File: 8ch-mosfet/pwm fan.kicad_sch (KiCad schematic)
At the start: 4 parts, among them M1 Fan_4pin

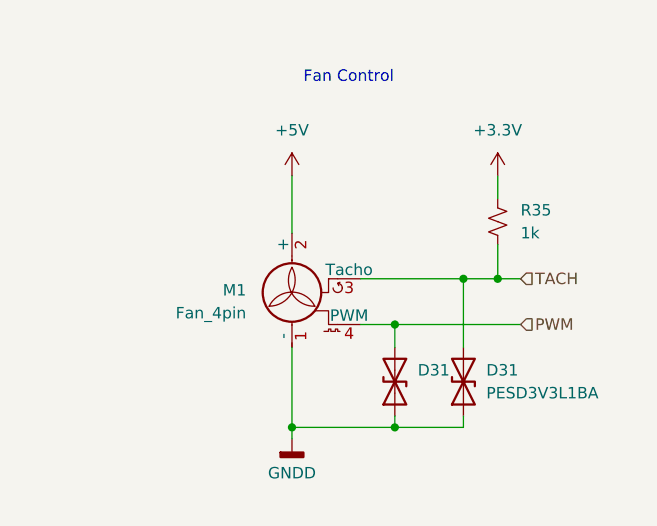
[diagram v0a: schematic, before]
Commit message: changed to MCP3564
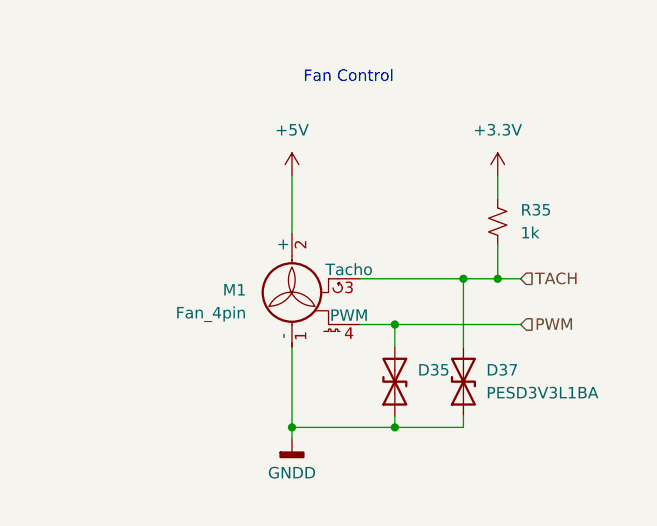
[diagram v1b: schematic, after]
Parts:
- renumbered D31 to D35, D31 to D37

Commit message: more progress on new 8ch board.
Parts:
- added Q17: 2N7002, Package_TO_SOT_SMD:SOT-23, symbol Transistor_FET:2N7002
- added R43: 1k, Resistor_SMD:R_0805_2012Metric_Pad1.20x1.40mm_HandSolder, symbol Device:R_Small_US
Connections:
- net GNDD: now also Q17.2 (S); no longer M1.1 (-)
- new net: M1.1 (-), Q17.3 (D)
- new net: Q17.1 (G), R43.1
- new net MOSFET: R43.2
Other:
- moved on the sheet: D35, D37, M1, R35

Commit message: updated busbar design.
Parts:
- renumbered Q17 to Q18, R43 to R44
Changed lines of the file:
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@@
 		(on_board yes)
 		(dnp no)
-		(property "Reference" "Q17"
+		(property "Reference" "Q18"
 			(at 135.89 95.25 0)
 			(effects
@@
 		(dnp no)
 		(fields_autoplaced yes)
-		(property "Reference" "R43"
+		(property "Reference" "R44"
 			(at 119.38 90.17 90)
 			(effects

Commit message: big update - 12ch, volt adc, senders, etc.
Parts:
- renumbered D35 to D27, D37 to D28, M1 to M2, Q18 to Q34, R44 to R59, R35 to R60
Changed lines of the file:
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@@
 		(dnp no)
 		(fields_autoplaced yes)
-		(property "Reference" "R35"
+		(property "Reference" "R60"
 			(at 161.29 72.39 0)
 			(effects
@@
 			(project "8ch-mosfet"
 				(path "/c83c6236-96e9-46ad-9d7a-9e2efa4a7966/02f6e629-b0e2-41e8-b2e4-f0e125a92a71"
-					(reference "R35")
-					(unit 1)
-				)
-				(path "/c83c6236-96e9-46ad-9d7a-9e2efa4a7966/ad82ad0c-2ba8-4934-bb2a-ed6e11658eb2"
-					(reference "R36")
+					(reference "R60")
+					(unit 1)
+				)
+				(path "/c83c6236-96e9-46ad-9d7a-9e2efa4a7966/ad82ad0c-2ba8-4934-bb2a-ed6e11658eb2"
+					(reference "R58")
 					(unit 1)
 				)
@@
 		(on_board yes)
 		(dnp no)
-		(property "Reference" "D35"
+		(property "Reference" "D27"
 			(at 149.86 95.25 90)
 			(effects
@@
 			(project "8ch-mosfet"
 				(path "/c83c6236-96e9-46ad-9d7a-9e2efa4a7966/02f6e629-b0e2-41e8-b2e4-f0e125a92a71"
-					(reference "D35")
-					(unit 1)
-				)
-				(path "/c83c6236-96e9-46ad-9d7a-9e2efa4a7966/ad82ad0c-2ba8-4934-bb2a-ed6e11658eb2"
-					(reference "D34")
+					(reference "D27")
+					(unit 1)
+				)
+				(path "/c83c6236-96e9-46ad-9d7a-9e2efa4a7966/ad82ad0c-2ba8-4934-bb2a-ed6e11658eb2"
+					(reference "D25")
 					(unit 1)
 				)
@@
 		(dnp no)
 		(fields_autoplaced yes)
-		(property "Reference" "#PWR064"
+		(property "Reference" "#PWR052"
 			(at 158.75 72.39 0)
 			(effects
@@
 			(project "8ch-mosfet"
 				(path "/c83c6236-96e9-46ad-9d7a-9e2efa4a7966/02f6e629-b0e2-41e8-b2e4-f0e125a92a71"
-					(reference "#PWR064")
-					(unit 1)
-				)
-				(path "/c83c6236-96e9-46ad-9d7a-9e2efa4a7966/ad82ad0c-2ba8-4934-bb2a-ed6e11658eb2"
-					(reference "#PWR066")
+					(reference "#PWR052")
+					(unit 1)
+				)
+				(path "/c83c6236-96e9-46ad-9d7a-9e2efa4a7966/ad82ad0c-2ba8-4934-bb2a-ed6e11658eb2"
+					(reference "#PWR049")
 					(unit 1)
 				)
@@
 		(on_board yes)
 		(dnp no)
-		(property "Reference" "M1"
+		(property "Reference" "M2"
 			(at 128.27 81.28 0)
 			(effects
@@
 			(project "8ch-mosfet"
 				(path "/c83c6236-96e9-46ad-9d7a-9e2efa4a7966/02f6e629-b0e2-41e8-b2e4-f0e125a92a71"
+					(reference "M2")
+					(unit 1)
+				)
+				(path "/c83c6236-96e9-46ad-9d7a-9e2efa4a7966/ad82ad0c-2ba8-4934-bb2a-ed6e11658eb2"
 					(reference "M1")
-					(unit 1)
-				)
-				(path "/c83c6236-96e9-46ad-9d7a-9e2efa4a7966/ad82ad0c-2ba8-4934-bb2a-ed6e11658eb2"
-					(reference "M2")
 					(unit 1)
 				)
@@
 		(dnp no)
 		(fields_autoplaced yes)
-		(property "Reference" "#PWR053"
+		(property "Reference" "#PWR051"
 			(at 133.35 111.76 0)
 			(effects
@@
 			(project "8ch-mosfet"
 				(path "/c83c6236-96e9-46ad-9d7a-9e2efa4a7966/02f6e629-b0e2-41e8-b2e4-f0e125a92a71"
-					(reference "#PWR053")
-					(unit 1)
-				)
-				(path "/c83c6236-96e9-46ad-9d7a-9e2efa4a7966/ad82ad0c-2ba8-4934-bb2a-ed6e11658eb2"
-					(reference "#PWR065")
+					(reference "#PWR051")
+					(unit 1)
+				)
+				(path "/c83c6236-96e9-46ad-9d7a-9e2efa4a7966/ad82ad0c-2ba8-4934-bb2a-ed6e11658eb2"
+					(reference "#PWR048")
 					(unit 1)
 				)
@@
 		(on_board yes)
 		(dnp no)
-		(property "Reference" "Q18"
+		(property "Reference" "Q34"
 			(at 135.89 95.25 0)
 			(effects
@@
 			(project "8ch-mosfet"
 				(path "/c83c6236-96e9-46ad-9d7a-9e2efa4a7966/02f6e629-b0e2-41e8-b2e4-f0e125a92a71"
-					(reference "Q18")
-					(unit 1)
-				)
-				(path "/c83c6236-96e9-46ad-9d7a-9e2efa4a7966/ad82ad0c-2ba8-4934-bb2a-ed6e11658eb2"
-					(reference "Q17")
+					(reference "Q34")
+					(unit 1)
+				)
+				(path "/c83c6236-96e9-46ad-9d7a-9e2efa4a7966/ad82ad0c-2ba8-4934-bb2a-ed6e11658eb2"
+					(reference "Q33")
 					(unit 1)
 				)
@@
 		(dnp no)
 		(fields_autoplaced yes)
-		(property "Reference" "#PWR08"
+		(property "Reference" "#PWR050"
 			(at 133.35 72.39 0)
 			(effects
@@
 			(project "8ch-mosfet"
 				(path "/c83c6236-96e9-46ad-9d7a-9e2efa4a7966/02f6e629-b0e2-41e8-b2e4-f0e125a92a71"
-					(reference "#PWR08")
-					(unit 1)
-				)
-				(path "/c83c6236-96e9-46ad-9d7a-9e2efa4a7966/ad82ad0c-2ba8-4934-bb2a-ed6e11658eb2"
-					(reference "#PWR063")
+					(reference "#PWR050")
+					(unit 1)
+				)
+				(path "/c83c6236-96e9-46ad-9d7a-9e2efa4a7966/ad82ad0c-2ba8-4934-bb2a-ed6e11658eb2"
+					(reference "#PWR047")
 					(unit 1)
 				)
@@
 		(on_board yes)
 		(dnp no)
-		(property "Reference" "D37"
+		(property "Reference" "D28"
 			(at 157.48 95.25 90)
 			(effects
@@
 			(project "8ch-mosfet"
 				(path "/c83c6236-96e9-46ad-9d7a-9e2efa4a7966/02f6e629-b0e2-41e8-b2e4-f0e125a92a71"
-					(reference "D37")
-					(unit 1)
-				)
-				(path "/c83c6236-96e9-46ad-9d7a-9e2efa4a7966/ad82ad0c-2ba8-4934-bb2a-ed6e11658eb2"
-					(reference "D36")
+					(reference "D28")
+					(unit 1)
+				)
+				(path "/c83c6236-96e9-46ad-9d7a-9e2efa4a7966/ad82ad0c-2ba8-4934-bb2a-ed6e11658eb2"
+					(reference "D26")
 					(unit 1)
 				)
@@
 		(dnp no)
 		(fields_autoplaced yes)
-		(property "Reference" "R44"
+		(property "Reference" "R59"
 			(at 119.38 90.17 90)
 			(effects
@@
 			(project "8ch-mosfet"
 				(path "/c83c6236-96e9-46ad-9d7a-9e2efa4a7966/02f6e629-b0e2-41e8-b2e4-f0e125a92a71"
-					(reference "R44")
-					(unit 1)
-				)
-				(path "/c83c6236-96e9-46ad-9d7a-9e2efa4a7966/ad82ad0c-2ba8-4934-bb2a-ed6e11658eb2"
-					(reference "R43")
-					(unit 1)
-				)
+					(reference "R59")
+					(unit 1)
+				)
+				(path "/c83c6236-96e9-46ad-9d7a-9e2efa4a7966/ad82ad0c-2ba8-4934-bb2a-ed6e11658eb2"
+					(reference "R57")
+					(unit 1)
+				)

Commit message: component layout looking crispy.
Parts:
- renumbered M2 to FAN2, R59 to R61, R60 to R62
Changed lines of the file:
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@@
 		(dnp no)
 		(fields_autoplaced yes)
-		(property "Reference" "R60"
+		(property "Reference" "R62"
 			(at 161.29 72.39 0)
 			(effects
@@
 			(project "8ch-mosfet"
 				(path "/c83c6236-96e9-46ad-9d7a-9e2efa4a7966/02f6e629-b0e2-41e8-b2e4-f0e125a92a71"
+					(reference "R62")
+					(unit 1)
+				)
+				(path "/c83c6236-96e9-46ad-9d7a-9e2efa4a7966/ad82ad0c-2ba8-4934-bb2a-ed6e11658eb2"
 					(reference "R60")
-					(unit 1)
-				)
-				(path "/c83c6236-96e9-46ad-9d7a-9e2efa4a7966/ad82ad0c-2ba8-4934-bb2a-ed6e11658eb2"
-					(reference "R58")
 					(unit 1)
 				)
@@
 		(dnp no)
 		(fields_autoplaced yes)
-		(property "Reference" "#PWR052"
+		(property "Reference" "#PWR053"
 			(at 158.75 72.39 0)
 			(effects
@@
 			(project "8ch-mosfet"
 				(path "/c83c6236-96e9-46ad-9d7a-9e2efa4a7966/02f6e629-b0e2-41e8-b2e4-f0e125a92a71"
-					(reference "#PWR052")
-					(unit 1)
-				)
-				(path "/c83c6236-96e9-46ad-9d7a-9e2efa4a7966/ad82ad0c-2ba8-4934-bb2a-ed6e11658eb2"
-					(reference "#PWR049")
+					(reference "#PWR053")
+					(unit 1)
+				)
+				(path "/c83c6236-96e9-46ad-9d7a-9e2efa4a7966/ad82ad0c-2ba8-4934-bb2a-ed6e11658eb2"
+					(reference "#PWR050")
 					(unit 1)
 				)
@@
 		(on_board yes)
 		(dnp no)
-		(property "Reference" "M2"
+		(property "Reference" "FAN2"
 			(at 128.27 81.28 0)
 			(effects
@@
 			(project "8ch-mosfet"
 				(path "/c83c6236-96e9-46ad-9d7a-9e2efa4a7966/02f6e629-b0e2-41e8-b2e4-f0e125a92a71"
-					(reference "M2")
-					(unit 1)
-				)
-				(path "/c83c6236-96e9-46ad-9d7a-9e2efa4a7966/ad82ad0c-2ba8-4934-bb2a-ed6e11658eb2"
-					(reference "M1")
+					(reference "FAN2")
+					(unit 1)
+				)
+				(path "/c83c6236-96e9-46ad-9d7a-9e2efa4a7966/ad82ad0c-2ba8-4934-bb2a-ed6e11658eb2"
+					(reference "FAN1")
 					(unit 1)
 				)
@@
 		(dnp no)
 		(fields_autoplaced yes)
-		(property "Reference" "#PWR051"
+		(property "Reference" "#PWR052"
 			(at 133.35 111.76 0)
 			(effects
@@
 			(project "8ch-mosfet"
 				(path "/c83c6236-96e9-46ad-9d7a-9e2efa4a7966/02f6e629-b0e2-41e8-b2e4-f0e125a92a71"
-					(reference "#PWR051")
-					(unit 1)
-				)
-				(path "/c83c6236-96e9-46ad-9d7a-9e2efa4a7966/ad82ad0c-2ba8-4934-bb2a-ed6e11658eb2"
-					(reference "#PWR048")
+					(reference "#PWR052")
+					(unit 1)
+				)
+				(path "/c83c6236-96e9-46ad-9d7a-9e2efa4a7966/ad82ad0c-2ba8-4934-bb2a-ed6e11658eb2"
+					(reference "#PWR049")
 					(unit 1)
 				)
@@
 		(dnp no)
 		(fields_autoplaced yes)
-		(property "Reference" "#PWR050"
+		(property "Reference" "#PWR051"
 			(at 133.35 72.39 0)
 			(effects
@@
 			(project "8ch-mosfet"
 				(path "/c83c6236-96e9-46ad-9d7a-9e2efa4a7966/02f6e629-b0e2-41e8-b2e4-f0e125a92a71"
-					(reference "#PWR050")
-					(unit 1)
-				)
-				(path "/c83c6236-96e9-46ad-9d7a-9e2efa4a7966/ad82ad0c-2ba8-4934-bb2a-ed6e11658eb2"
-					(reference "#PWR047")
+					(reference "#PWR051")
+					(unit 1)
+				)
+				(path "/c83c6236-96e9-46ad-9d7a-9e2efa4a7966/ad82ad0c-2ba8-4934-bb2a-ed6e11658eb2"
+					(reference "#PWR048")
 					(unit 1)
 				)
@@
 		(dnp no)
 		(fields_autoplaced yes)
-		(property "Reference" "R59"
+		(property "Reference" "R61"
 			(at 119.38 90.17 90)
 			(effects
@@
 			(project "8ch-mosfet"
 				(path "/c83c6236-96e9-46ad-9d7a-9e2efa4a7966/02f6e629-b0e2-41e8-b2e4-f0e125a92a71"
+					(reference "R61")
+					(unit 1)
+				)
+				(path "/c83c6236-96e9-46ad-9d7a-9e2efa4a7966/ad82ad0c-2ba8-4934-bb2a-ed6e11658eb2"
 					(reference "R59")
 					(unit 1)
 				)
-				(path "/c83c6236-96e9-46ad-9d7a-9e2efa4a7966/ad82ad0c-2ba8-4934-bb2a-ed6e11658eb2"
-					(reference "R57")
-					(unit 1)
-				)
